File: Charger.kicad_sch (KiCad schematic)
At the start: 55 parts, among them Q6 BSC0702LS, Q7 BSC0702LS, Q8 BSC0702LS, Q9 BSC0702LS, U27 BQ25756RRVR

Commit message: Fixed resistor values, small changes
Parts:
- R23: value 140kR -> 15k 0.1%; JLC C185372 -> C2692707
- R71: value 140kR -> 220kR 0.1%; JLC C185372 -> C861231
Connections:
- net 3.3V renamed 5V
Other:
- note added: "RBot = 14.04 kOhms gives 4.12V cell end voltage. 14.04 = 220k and 15k in parallel"
- moved on the sheet: D29, D5, D6, JP1, R34, R35, R72, R73, R76, TP1

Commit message: updated gate charger resistor value
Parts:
- R66: value 120R -> 0R; JLC C17437 -> C17477

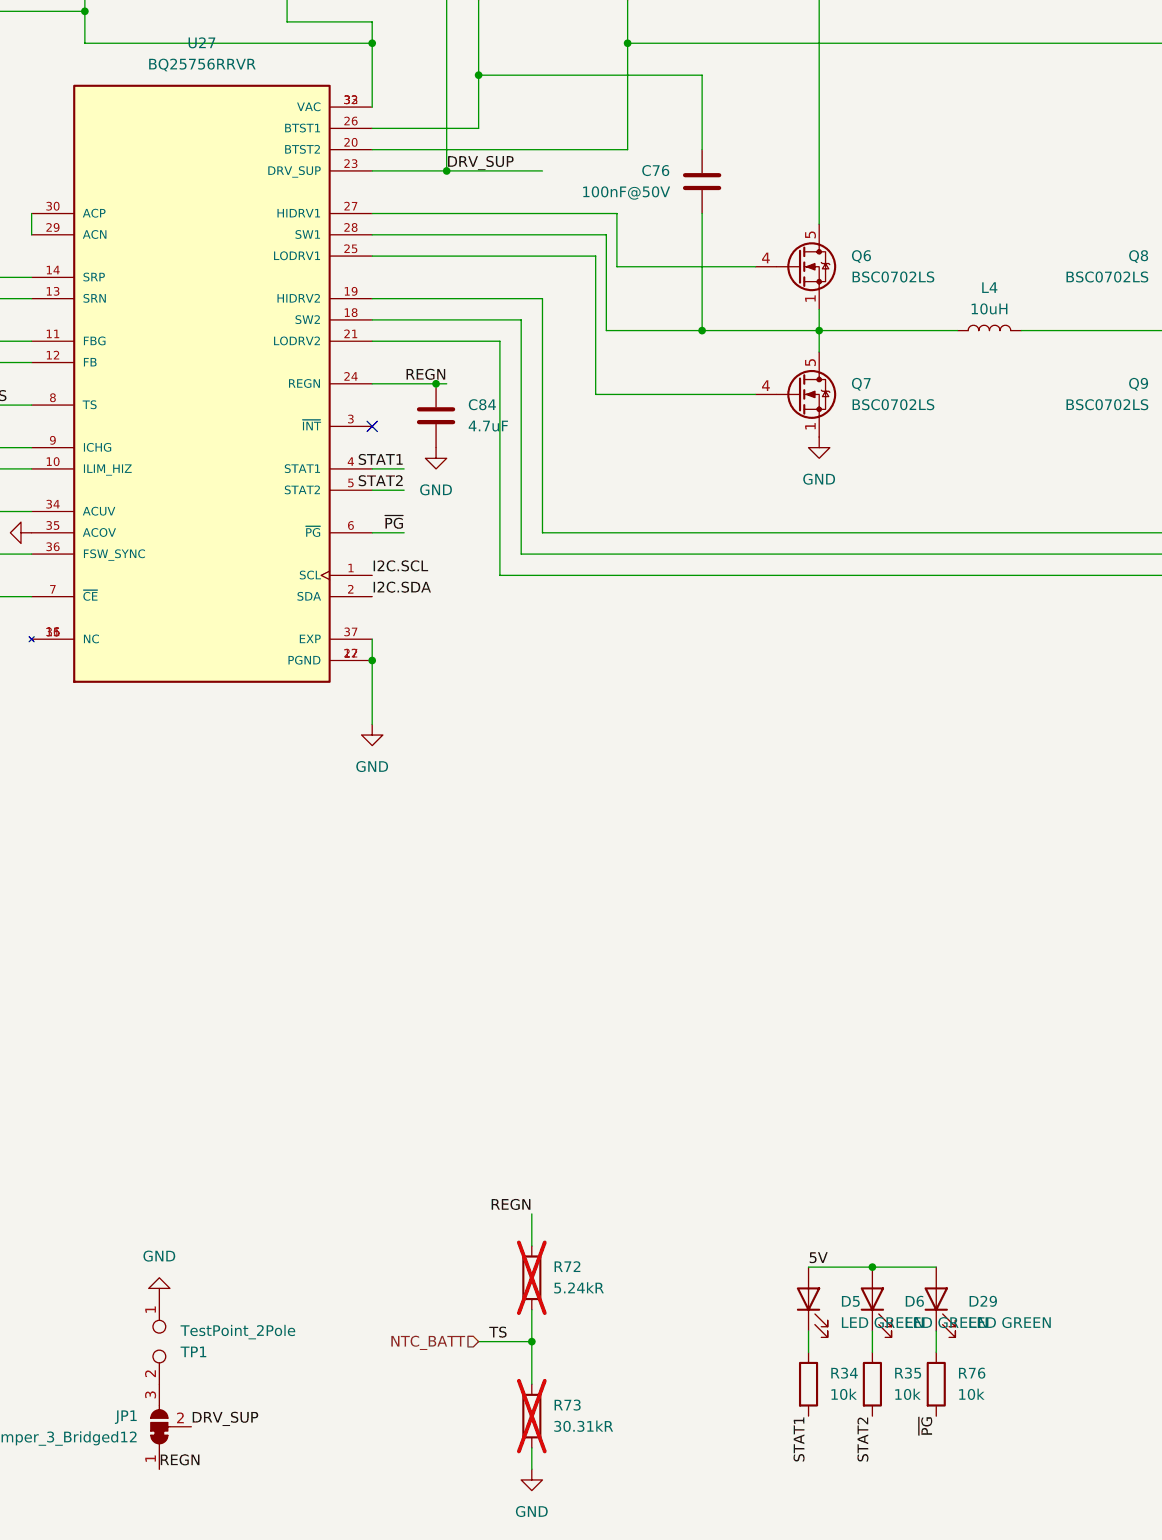
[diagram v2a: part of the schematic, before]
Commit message: Make ERC happy
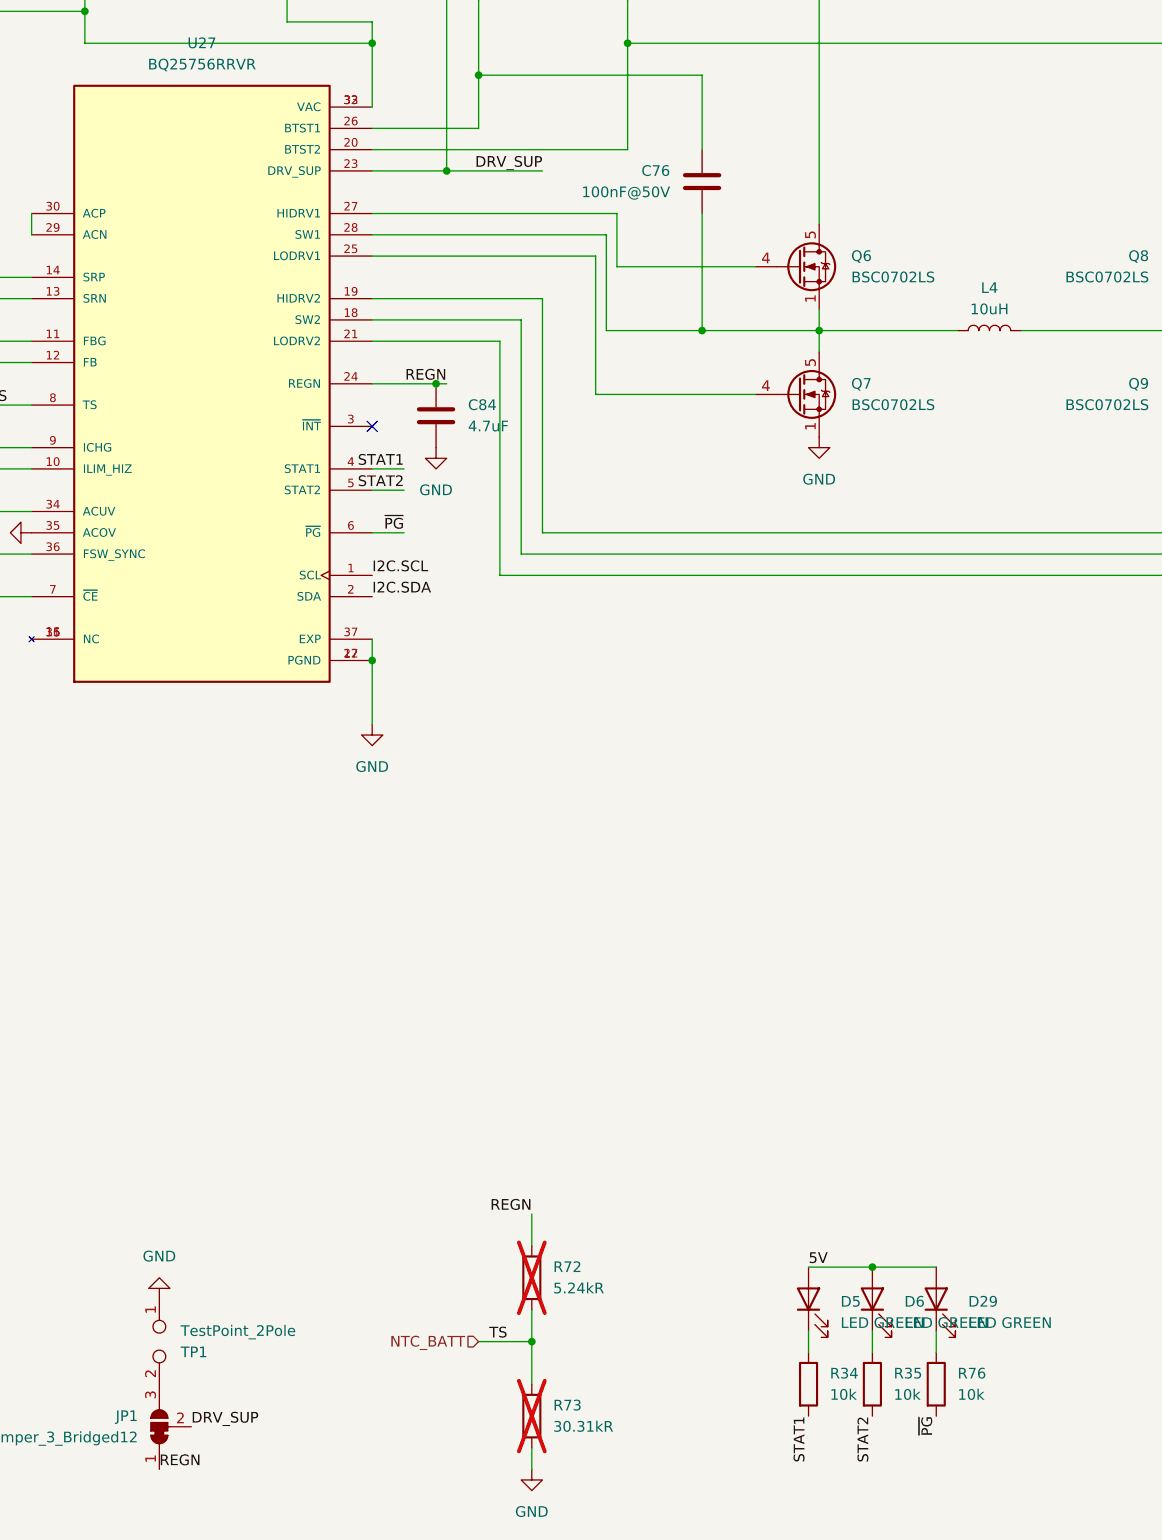
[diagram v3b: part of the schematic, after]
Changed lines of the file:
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@@
 (kicad_sch
-	(version 20231120)
+	(version 20250114)
 	(generator "eeschema")
-	(generator_version "8.0")
+	(generator_version "9.0")
 	(paper "A3")
+	(text "RBot = 14.04 kOhms gives 4.12V cell end voltage.\n14.04 = 220k and 15k in parallel"
+		(exclude_from_sim no)
+		(at 414.274 164.338 0)
+		(effects
+			(font
+				(size 1.27 1.27)
+			)
+			(justify left)
+		)
+	)
 	(junction
 		(at 336.55 132.08)
@@
 		)
 	)
-	(text "RBot = 14.04 kOhms gives 4.12V cell end voltage.\n14.04 = 220k and 15k in parallel"
-		(exclude_from_sim no)
-		(at 414.274 164.338 0)
-		(effects
-			(font
-				(size 1.27 1.27)
-			)
-			(justify left)
-		)
-	)
 	(label "TS"
 		(at 139.7 146.05 0)
-		(fields_autoplaced yes)
 		(effects
 			(font
@@
 	(label "REGN"
 		(at 160.02 273.05 0)
-		(fields_autoplaced yes)
 		(effects
 			(font
@@
 	(label "SRP"
 		(at 118.11 130.81 0)
-		(fields_autoplaced yes)
 		(effects
 			(font
@@
 	(label "STAT1"
 		(at 189.23 153.67 180)
-		(fields_autoplaced yes)
 		(effects
 			(font
@@
 	(label "5V"
 		(at 62.23 255.27 180)
-		(fields_autoplaced yes)
 		(effects
 			(font
@@
 	(label "REGN"
 		(at 194.31 143.51 180)
-		(fields_autoplaced yes)
 		(effects
 			(font
@@
 	(label "FB"
 		(at 139.7 140.97 180)
-		(fields_autoplaced yes)
 		(effects
 			(font
@@
 	(label "SRP"
 		(at 372.11 161.29 0)
-		(fields_autoplaced yes)
 		(effects
 			(font
@@
 	)
 	(label "DRV_SUP"
-		(at 194.31 118.11 0)
-		(fields_autoplaced yes)
+		(at 205.74 118.11 180)
 		(effects
 			(font
 				(size 1.27 1.27)
 			)
-			(justify left bottom)
+			(justify right bottom)
 		)
 	)
 	(label "TS"
 		(at 199.39 257.81 0)
-		(fields_autoplaced yes)
 		(effects
 			(font
@@
 	(label "5V"
 		(at 237.49 248.92 0)
-		(fields_autoplaced yes)
 		(effects
 			(font
@@
 	(label "I2C.SDA"
 		(at 185.42 168.91 0)
-		(fields_autoplaced yes)
 		(effects
 			(font
@@
 	(label "SRN"
 		(at 118.11 133.35 0)
-		(fields_autoplaced yes)
 		(effects
 			(font
@@
 	(label "STAT2"
 		(at 189.23 156.21 180)
-		(fields_autoplaced yes)
 		(effects
 			(font
@@
 	(label "~{PG}"
 		(at 252.73 266.7 270)
-		(fields_autoplaced yes)
 		(effects
 			(font
@@
 	(label "STAT2"
 		(at 245.11 266.7 270)
-		(fields_autoplaced yes)
 		(effects
 			(font
@@
 	(label "~{PG}"
 		(at 189.23 161.29 180)
-		(fields_autoplaced yes)
 		(effects
 			(font
@@
 	(label "FB"
 		(at 422.91 135.89 0)
-		(fields_autoplaced yes)
 		(effects
 			(font
@@
 	(label "STAT1"
 		(at 237.49 266.7 270)
-		(fields_autoplaced yes)
 		(effects
 			(font
@@
 	(label "I2C.SCL"
 		(at 185.42 166.37 0)
-		(fields_autoplaced yes)
 		(effects
 			(font
@@
 	(label "DRV_SUP"
 		(at 163.83 267.97 0)
-		(fields_autoplaced yes)
 		(effects
 			(font
@@
 	(label "FBG"
 		(at 422.91 156.21 0)
-		(fields_autoplaced yes)
 		(effects
 			(font
@@
 	(label "REGN"
 		(at 204.47 242.57 180)
-		(fields_autoplaced yes)
 		(effects
 			(font
@@
 	(label "FBG"
 		(at 139.7 138.43 180)
-		(fields_autoplaced yes)
 		(effects
 			(font
@@
 	(label "SRN"
 		(at 401.32 161.29 0)
-		(fields_autoplaced yes)
 		(effects
 			(font
@@
 		(shape input)
 		(at 46.99 255.27 180)
-		(fields_autoplaced yes)
 		(effects
 			(font
@@
 		(shape output)
 		(at 478.79 124.46 0)
-		(fields_autoplaced yes)
 		(effects
 			(font
@@
 		(shape input)
 		(at 198.12 257.81 180)
-		(fields_autoplaced yes)
 		(effects
 			(font
@@
 		(shape input)
 		(at 46.99 262.89 180)
-		(fields_autoplaced yes)
 		(effects
 			(font
@@
 		(shape input)
 		(at 36.83 55.88 180)
-		(fields_autoplaced yes)
 		(effects
 			(font
@@
 			)
 		)
+		(property "Sim.Pins" "1=K 2=A"
+			(at 245.11 252.73 0)
+			(effects
+				(font
+					(size 1.27 1.27)
+				)
+				(hide yes)
+			)
+		)
 		(pin "2"
 		)
@@
 			)
 		)
+		(property "Sim.Pins" "1=K 2=A"
+			(at 252.73 252.73 0)
+			(effects
+				(font
+					(size 1.27 1.27)
+				)
+				(hide yes)
+			)
+		)
 		(pin "2"
 		)
@@
 			(at 237.49 252.73 0)
 			(effects
+				(font
+					(size 1.27 1.27)
+				)
+				(hide yes)
+			)
+		)
+		(property "Sim.Pins" "1=K 2=A"
+			(at 237.49 252.73 0)
+			(effects

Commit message: Compact charger for USB move
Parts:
- C55, C56, C58, C59: footprint Capacitor_SMD:C_1206_3216Metric -> Capacitor_SMD:C_0805_2012Metric; JLC C29823 -> C2991173
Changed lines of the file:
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@@
 			)
 		)
-		(property "Footprint" "Capacitor_SMD:C_1206_3216Metric"
+		(property "Footprint" "Capacitor_SMD:C_0805_2012Metric"
 			(at 337.5152 132.08 0)
 			(effects
@@
 			)
 		)
-		(property "Description" "Unpolarized capacitor"
+		(property "Description" "4.7uF 50V X7R ±10% 0805 Multilayer Ceramic Capacitors MLCC - SMD/SMT ROHS"
 			(at 336.55 128.27 0)
 			(effects
@@
 			)
 		)
-		(property "JLC" "C29823"
+		(property "JLC" "C2991173"
 			(at 336.55 128.27 0)
 			(effects
@@
 			)
 		)
-		(property "Footprint" "Capacitor_SMD:C_1206_3216Metric"
+		(property "Footprint" "Capacitor_SMD:C_0805_2012Metric"
 			(at 332.4352 132.08 0)
 			(effects
@@
 			)
 		)
-		(property "Description" "Unpolarized capacitor"
+		(property "Description" "4.7uF 50V X7R ±10% 0805 Multilayer Ceramic Capacitors MLCC - SMD/SMT ROHS"
 			(at 331.47 128.27 0)
 			(effects
@@
 			)
 		)
-		(property "JLC" "C29823"
+		(property "JLC" "C2991173"
 			(at 331.47 128.27 0)
 			(effects
@@
 			)
 		)
-		(property "Footprint" "Capacitor_SMD:C_1206_3216Metric"
+		(property "Footprint" "Capacitor_SMD:C_0805_2012Metric"
 			(at 327.3552 132.08 0)
 			(effects
@@
 			)
 		)
-		(property "Description" "Unpolarized capacitor"
+		(property "Description" "4.7uF 50V X7R ±10% 0805 Multilayer Ceramic Capacitors MLCC - SMD/SMT ROHS"
 			(at 326.39 128.27 0)
 			(effects
@@
 			)
 		)
-		(property "JLC" "C29823"
+		(property "JLC" "C2991173"
 			(at 326.39 128.27 0)
 			(effects
@@
 			)
 		)
-		(property "Footprint" "Capacitor_SMD:C_1206_3216Metric"
+		(property "Footprint" "Capacitor_SMD:C_0805_2012Metric"
 			(at 322.2752 132.08 0)
 			(effects
@@
 			)
 		)
-		(property "Description" "Unpolarized capacitor"
+		(property "Description" "4.7uF 50V X7R ±10% 0805 Multilayer Ceramic Capacitors MLCC - SMD/SMT ROHS"
 			(at 321.31 128.27 0)
 			(effects
@@
 			)
 		)
-		(property "JLC" "C29823"
+		(property "JLC" "C2991173"
 			(at 321.31 128.27 0)
 			(effects

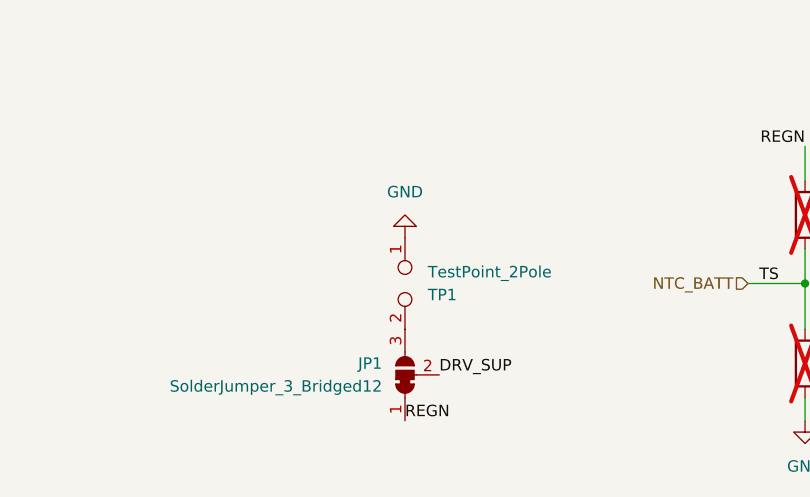
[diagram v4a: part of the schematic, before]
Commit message: Fix BOM and switch C0402 to C0603
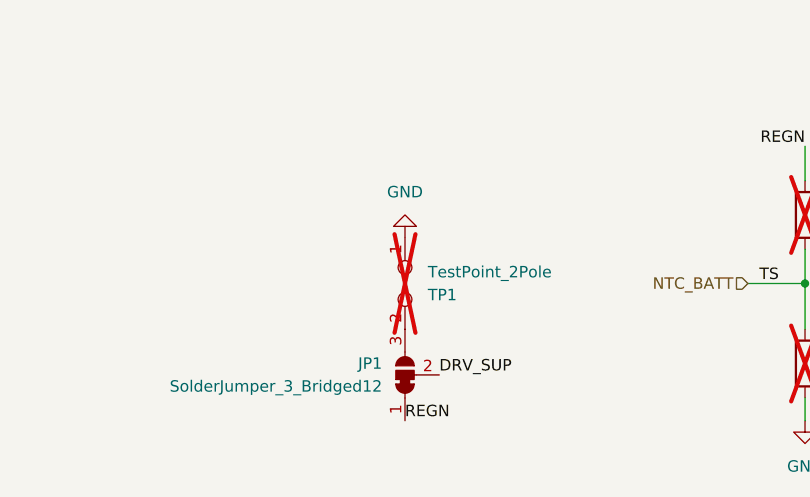
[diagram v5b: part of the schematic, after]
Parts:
- R21: footprint Resistor_SMD:R_0402_1005Metric -> Resistor_SMD:R_0603_1608Metric; JLC C25741 -> C25803
- R75: footprint Resistor_SMD:R_0402_1005Metric -> Resistor_SMD:R_0603_1608Metric; JLC C25744 -> C25804
- TP1: now not fitted; now left out of the parts list
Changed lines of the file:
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@@
 		(unit 1)
 		(exclude_from_sim no)
-		(in_bom yes)
+		(in_bom no)
 		(on_board yes)
-		(dnp no)
+		(dnp yes)
 		(property "Reference" "TP1"
 			(at 162.56 259.0801 90)
@@
 			)
 		)
-		(property "Footprint" "Resistor_SMD:R_0402_1005Metric"
+		(property "Footprint" "Resistor_SMD:R_0603_1608Metric"
 			(at 108.712 175.26 90)
 			(effects
@@
 			)
 		)
-		(property "JLC" "C25744"
+		(property "JLC" "C25804"
 			(at 110.49 175.26 0)
 			(effects
@@
 			)
 		)
-		(property "Footprint" "Resistor_SMD:R_0402_1005Metric"
+		(property "Footprint" "Resistor_SMD:R_0603_1608Metric"
 			(at 90.932 161.29 90)
 			(effects
@@
 			)
 		)
-		(property "JLC" "C25741"
+		(property "JLC" "C25803"
 			(at 92.71 161.29 0)
 			(effects

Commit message: Switch R0402 to 0603
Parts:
- R34, R35, R76: footprint Resistor_SMD:R_0402_1005Metric -> Resistor_SMD:R_0603_1608Metric; JLC C25744 -> C25804
- R68, R69: footprint Resistor_SMD:R_0402_1005Metric -> Resistor_SMD:R_0603_1608Metric; JLC C25077 -> C22859
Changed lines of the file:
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@@
 			)
 		)
-		(property "Footprint" "Resistor_SMD:R_0402_1005Metric"
+		(property "Footprint" "Resistor_SMD:R_0603_1608Metric"
 			(at 250.952 262.89 90)
 			(effects
@@
 			)
 		)
-		(property "JLC" "C25744"
+		(property "JLC" "C25804"
 			(at 252.73 262.89 0)
 			(effects
@@
 			)
 		)
-		(property "Footprint" "Resistor_SMD:R_0402_1005Metric"
+		(property "Footprint" "Resistor_SMD:R_0603_1608Metric"
 			(at 399.542 128.27 90)
 			(effects
@@
 			)
 		)
-		(property "JLC" "C25077"
+		(property "JLC" "C22859"
 			(at 401.32 128.27 0)
 			(effects
@@
 			)
 		)
-		(property "Footprint" "Resistor_SMD:R_0402_1005Metric"
+		(property "Footprint" "Resistor_SMD:R_0603_1608Metric"
 			(at 235.712 262.89 90)
 			(effects
@@
 			)
 		)
-		(property "JLC" "C25744"
+		(property "JLC" "C25804"
 			(at 237.49 262.89 0)
 			(effects
@@
 			)
 		)
-		(property "Footprint" "Resistor_SMD:R_0402_1005Metric"
+		(property "Footprint" "Resistor_SMD:R_0603_1608Metric"
 			(at 243.332 262.89 90)
 			(effects
@@
 			)
 		)
-		(property "JLC" "C25744"
+		(property "JLC" "C25804"
 			(at 245.11 262.89 0)
 			(effects
@@
 			)
 		)
-		(property "Footprint" "Resistor_SMD:R_0402_1005Metric"
+		(property "Footprint" "Resistor_SMD:R_0603_1608Metric"
 			(at 370.332 128.27 90)
 			(effects
@@
 			)
 		)
-		(property "JLC" "C25077"
+		(property "JLC" "C22859"
 			(at 372.11 128.27 0)
 			(effects

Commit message: Fix BOM and parts placement
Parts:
- U27: FT Rotation Offset (none) -> -90
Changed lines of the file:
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@@
 			)
 		)
-		(property "APPLICATION" ""
+		(property "FT Rotation Offset" "-90"
 			(at 165.1 143.51 0)
 			(effects
